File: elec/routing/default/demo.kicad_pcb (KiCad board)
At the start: 4 copper layers, 25 x 25 mm, 34 parts, among them U1 ?, U2 ?, U3 ?, U4 ?, U5 ?, U6 KMR211NGLFS (Tactile Switches), U7 ?, U8 ?

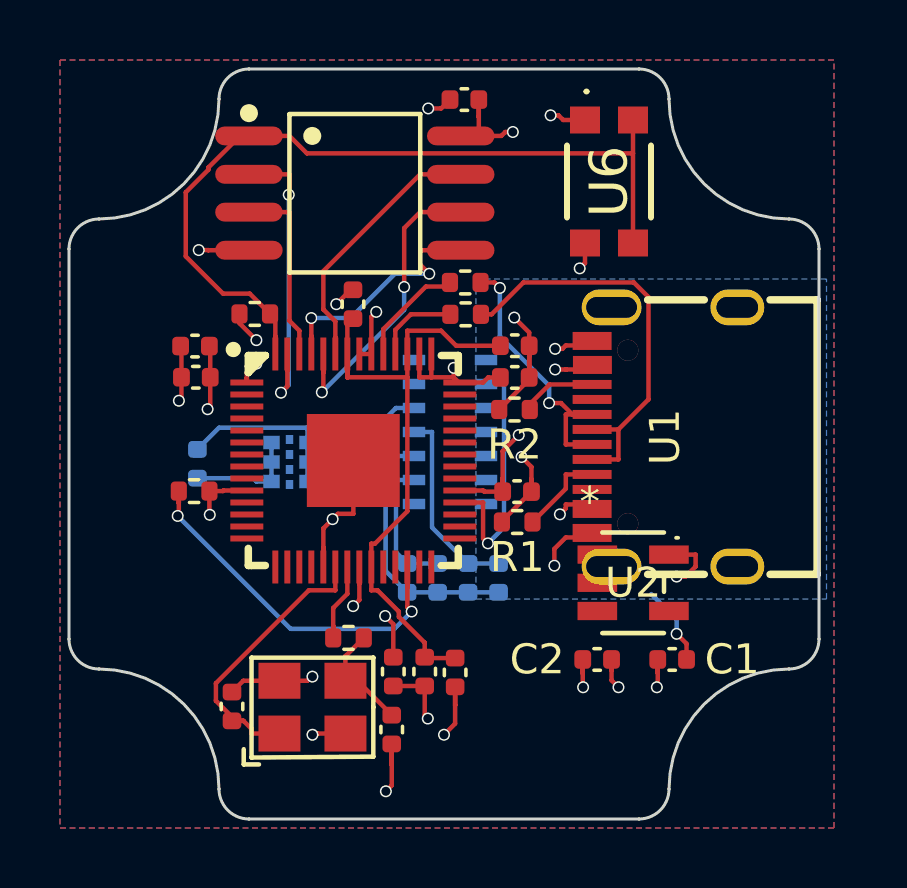
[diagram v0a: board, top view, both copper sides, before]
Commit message: [ELEC] messed up layout
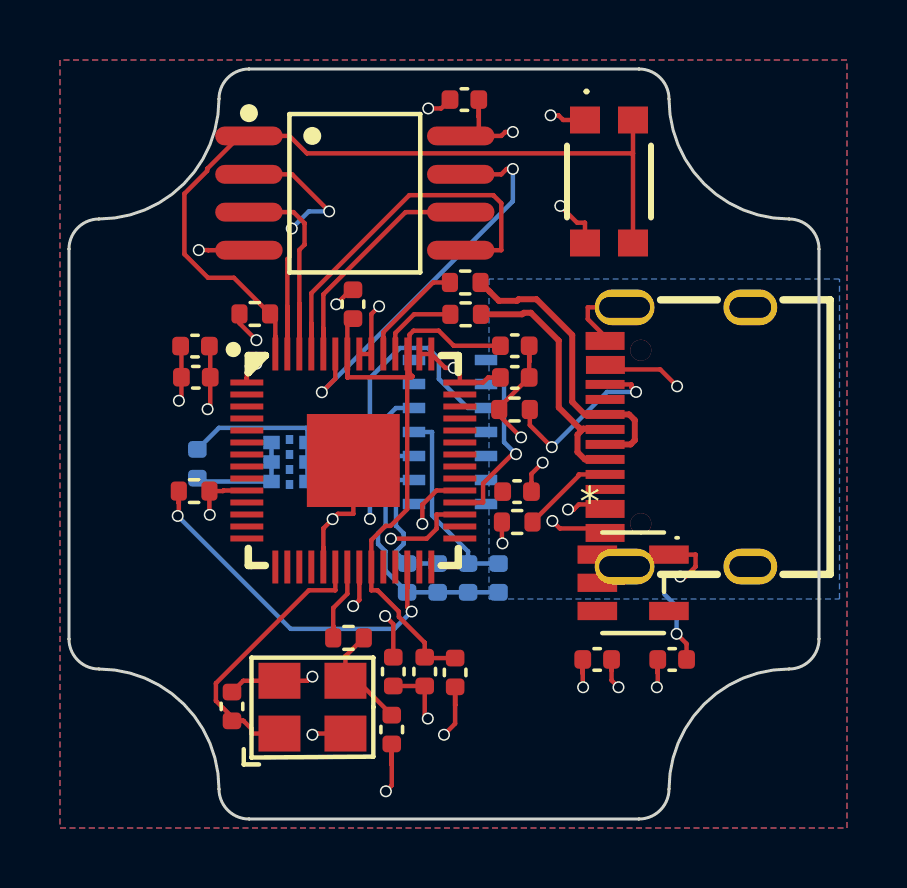
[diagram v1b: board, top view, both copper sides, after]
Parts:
- moved U1 0.43 mm to (150.3, 102.3)
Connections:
- net dm renamed usb_N
- net dp renamed usb_P
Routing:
- net sda: track 0.00 -> 14.1 mm, vias 0 -> 2
- net io0: track 8.60 -> 13.8 mm, vias 2 -> 0
- net usb_N: track 13.8 -> 8.96 mm
- net io3: track 9.39 -> 13.8 mm, vias 0 -> 2
- net cc2: track 2.53 -> 6.32 mm, vias 0 -> 2
- net power_supply-vcc: track 28.2 -> 24.7 mm
- net scl: track 8.34 -> 6.02 mm
- net usb_connector-gnd-1: track 38.6 -> 40.7 mm
- net microcontroller.rp2040-sck-1: track 10.6 -> 8.55 mm, vias 2 -> 0
- net usb_P: track 8.93 -> 10.8 mm, vias 2 -> 0
- net io2: track 6.61 -> 8.11 mm
- net microcontroller.rp2040.micro-vcc: track 21.7 -> 22.9 mm
- net usb_connector-vcc: track 6.06 -> 7.28 mm
